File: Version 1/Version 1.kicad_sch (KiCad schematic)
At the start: 82 parts, among them J1 Conn_01x05, Q1 IPP015N04NF2SAKMA1, Q2 IPP015N04NF2SAKMA1, Q3 IPP015N04NF2SAKMA1, Q4 IPP015N04NF2SAKMA1, Q5 IPP015N04NF2SAKMA1, Q6 IPP015N04NF2SAKMA1, U1 TPS62932, U2 TPS62932, U3 TPS62932, U4 IRS2004, U5 IRS2004, U6 IRS2004, U7 YAAJ_BlackPill_SWD_BreakoutV2, U8 Conn_01x01_Socket

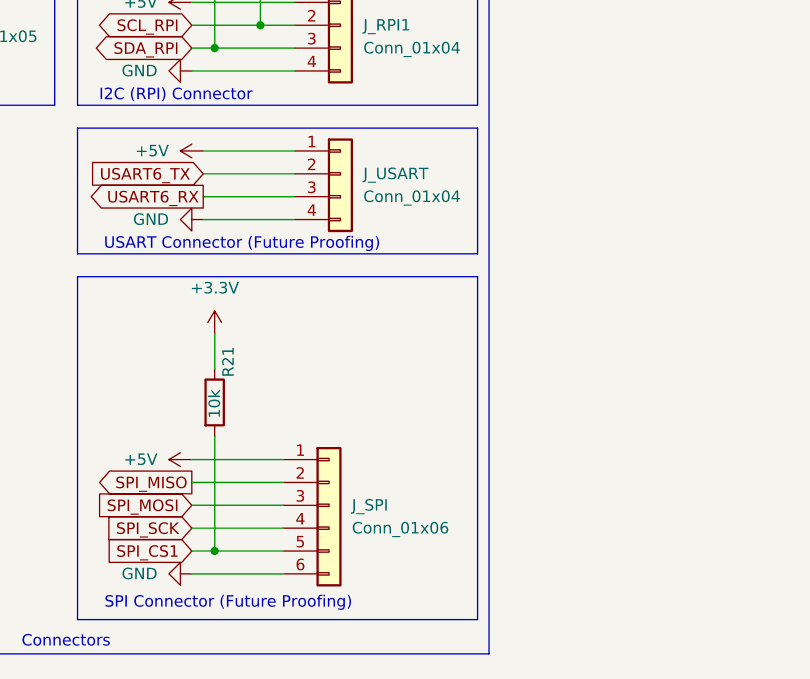
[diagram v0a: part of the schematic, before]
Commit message: Last few changes
Renamed a connector and added proper layout to the schematic.
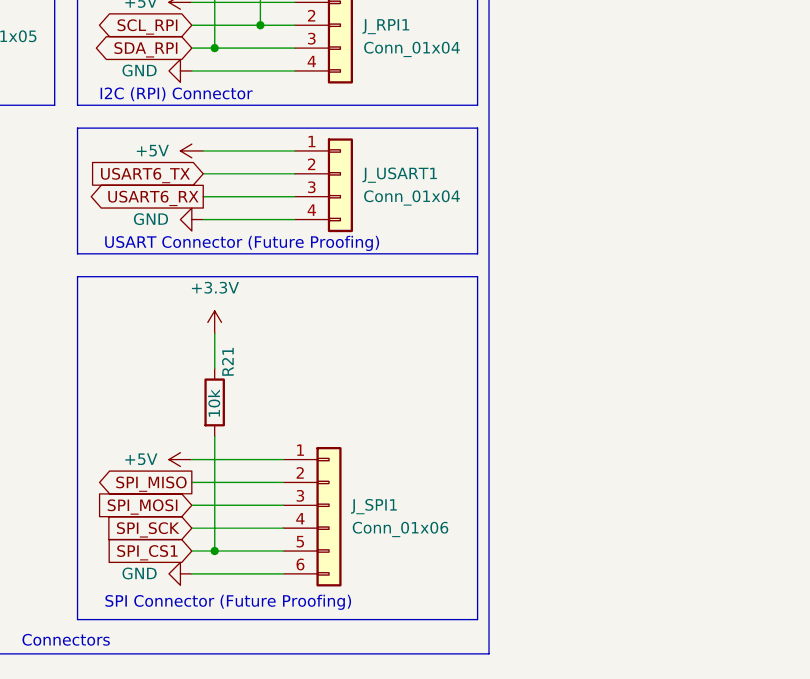
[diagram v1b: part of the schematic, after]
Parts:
- renumbered J_SPI to J_SPI1, J_USART to J_USART1
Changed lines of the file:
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@@
 		(dnp no)
 		(fields_autoplaced yes)
-		(property "Reference" "J_USART"
+		(property "Reference" "J_USART1"
 			(at 173.99 190.4999 0)
 			(effects
@@
 			(project "Version 1"
 				(path "/1b67c1a2-c765-4a1d-8ccd-1a2054fe1222"
-					(reference "J_USART")
+					(reference "J_USART1")
 					(unit 1)
 				)
@@
 		(dnp no)
 		(fields_autoplaced yes)
-		(property "Reference" "J_SPI"
+		(property "Reference" "J_SPI1"
 			(at 172.72 227.3299 0)
 			(effects
@@
 			(project "Version 1"
 				(path "/1b67c1a2-c765-4a1d-8ccd-1a2054fe1222"
-					(reference "J_SPI")
-					(unit 1)
-				)
+					(reference "J_SPI1")
+					(unit 1)
+				)

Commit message: updated footprints and added pos in pcb design
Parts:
- J_RPI1, J_USART1: footprint Connector_JST:JST_ACH_BM04B-ACHSS-A-GAN-ETF_1x04-1MP_P1.20mm_Vertical -> Connector_PinHeader_1.27mm:PinHeader_1x04_P1.27mm_Vertical
- J_SPI1: footprint (none) -> Connector_PinHeader_1.27mm:PinHeader_1x06_P1.27mm_Vertical
- R19, R20, R21: footprint (none) -> Resistor_THT:R_Axial_DIN0207_L6.3mm_D2.5mm_P10.16mm_Horizontal
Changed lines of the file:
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@@
 			)
 		)
-		(property "Footprint" "Connector_JST:JST_ACH_BM04B-ACHSS-A-GAN-ETF_1x04-1MP_P1.20mm_Vertical"
+		(property "Footprint" "Connector_PinHeader_1.27mm:PinHeader_1x04_P1.27mm_Vertical"
 			(at 171.45 190.5 0)
 			(effects
@@
 			)
 		)
-		(property "Footprint" ""
+		(property "Footprint" "Resistor_THT:R_Axial_DIN0207_L6.3mm_D2.5mm_P10.16mm_Horizontal"
 			(at 160.782 165.1 90)
 			(effects
@@
 			)
 		)
-		(property "Footprint" ""
+		(property "Footprint" "Connector_PinHeader_1.27mm:PinHeader_1x06_P1.27mm_Vertical"
 			(at 170.18 227.33 0)
 			(effects
@@
 			)
 		)
-		(property "Footprint" ""
+		(property "Footprint" "Resistor_THT:R_Axial_DIN0207_L6.3mm_D2.5mm_P10.16mm_Horizontal"
 			(at 155.702 165.1 90)
 			(effects
@@
 			)
 		)
-		(property "Footprint" "Connector_JST:JST_ACH_BM04B-ACHSS-A-GAN-ETF_1x04-1MP_P1.20mm_Vertical"
+		(property "Footprint" "Connector_PinHeader_1.27mm:PinHeader_1x04_P1.27mm_Vertical"
 			(at 171.45 173.99 0)
 			(effects
@@
 			)
 		)
-		(property "Footprint" ""
+		(property "Footprint" "Resistor_THT:R_Axial_DIN0207_L6.3mm_D2.5mm_P10.16mm_Horizontal"
 			(at 155.702 215.9 90)
 			(effects

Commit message: updated SCHEMATIC
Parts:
- added C10: 0.1u, symbol Device:C
- added C11: 1n, symbol Device:C
- added U8: ACS712xLCTR-05B, Package_SO:SOIC-8_3.9x4.9mm_P1.27mm, symbol Sensor_Current:ACS712xLCTR-05B
- renumbered U8 to OutU1, V1 to OutW1, W1 to OutW2
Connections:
- net +24V: now also U8.1 (IP+), U8.2 (IP+); no longer C5.1, C7.1, C9.1, Q1.2, Q3.2, Q5.2
- net +5V: now also C10.2, U8.8 (VCC)
- net ADC1: now also U8.7 (VIOUT)
- net GND: now also C10.1, C11.2, U8.5 (GND)
- net SH_U: no longer C4.2, Q1.3, Q2.2
- net SH_V: no longer C6.2, Q3.3, Q4.2
- net SH_W: no longer C8.2, Q5.3, Q6.2
- net at OutW2.1 (Pin_1): now also C8.2, Q5.3, Q6.2
- net at OutW1.1 (Pin_1): now also C6.2, Q3.3, Q4.2
- net at OutU1.1 (Pin_1): now also C4.2, Q1.3, Q2.2
- new net: C11.1, U8.6 (FILTER)
- new net 24V: C5.1, C7.1, C9.1, Q1.2, Q3.2, Q5.2, U8.3 (IP-), U8.4 (IP-)
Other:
- note added: "C12 is a function of the load resistance and filtering desired. R23 can be omitted if the full range is desired"
- note added: "Current sensing"
- moved on the sheet: OutU1, OutW1, OutW2

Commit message: updated
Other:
- note removed: "C12 is a function of the load resistance and filtering desired. R23 can be omitted if the full range is desired"
- moved on the sheet: C10, C11, D1, Jin1, Jout1, U8

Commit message: Nothing
Nothing
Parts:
- Rfbt3: value 30.9 -> 30.9k
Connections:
- net +5V: now also C10.1; no longer C10.2
- net GND: now also C10.2; no longer C10.1
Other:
- moved on the sheet: C10
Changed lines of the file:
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@@
 	)
 	(junction
-		(at 273.05 93.98)
+		(at 96.52 33.02)
 		(diameter 0)
 		(color 0 0 0 0)
 	)
 	(junction
-		(at 96.52 33.02)
+		(at 87.63 83.82)
 		(diameter 0)
 		(color 0 0 0 0)
 	)
 	(junction
-		(at 87.63 83.82)
+		(at 273.05 90.17)
 		(diameter 0)
 		(color 0 0 0 0)
@@
 	(wire
 		(pts
+			(xy 283.21 91.44) (xy 283.21 90.17)
+		)
+		(stroke
+			(width 0)
+			(type default)
+		)
+	)
+	(wire
+		(pts
 			(xy 166.37 187.96) (xy 156.21 187.96)
 		)
@@
 	(wire
 		(pts
-			(xy 271.78 93.98) (xy 273.05 93.98)
-		)
-		(stroke
-			(width 0)
-			(type default)
-		)
-	)
-	(wire
-		(pts
 			(xy 330.2 43.18) (xy 330.2 46.99)
 		)
@@
 	(wire
 		(pts
+			(xy 273.05 90.17) (xy 273.05 95.25)
+		)
+		(stroke
+			(width 0)
+			(type default)
+		)
+	)
+	(wire
+		(pts
 			(xy 30.48 120.65) (xy 30.48 121.92)
 		)
@@
 	(wire
 		(pts
+			(xy 274.32 90.17) (xy 273.05 90.17)
+		)
+		(stroke
+			(width 0)
+			(type default)
+		)
+	)
+	(wire
+		(pts
 			(xy 175.26 46.99) (xy 175.26 50.8)
 		)
@@
 	(wire
 		(pts
-			(xy 273.05 92.71) (xy 273.05 93.98)
-		)
-		(stroke
-			(width 0)
-			(type default)
-		)
-	)
-	(wire
-		(pts
 			(xy 25.4 121.92) (xy 30.48 121.92)
 		)
@@
 	(wire
 		(pts
-			(xy 273.05 93.98) (xy 273.05 95.25)
+			(xy 148.59 86.36) (xy 148.59 88.9)
 		)
 		(stroke
@@
 	(wire
 		(pts
-			(xy 148.59 86.36) (xy 148.59 88.9)
+			(xy 29.21 34.29) (xy 29.21 35.56)
 		)
 		(stroke
@@
 	(wire
 		(pts
-			(xy 29.21 34.29) (xy 29.21 35.56)
+			(xy 173.99 115.57) (xy 173.99 116.84)
 		)
 		(stroke
@@
 	(wire
 		(pts
-			(xy 173.99 115.57) (xy 173.99 116.84)
+			(xy 283.21 90.17) (xy 281.94 90.17)
 		)
 		(stroke
@@
 		(on_board yes)
 		(dnp no)
-		(fields_autoplaced yes)
 		(property "Reference" "#PWR029"
 			(at 212.09 88.9 0)
@@
 	(symbol
 		(lib_id "Device:C")
-		(at 273.05 88.9 0)
+		(at 278.13 90.17 90)
 		(unit 1)
 		(exclude_from_sim no)
@@
 		(on_board yes)
 		(dnp no)
-		(fields_autoplaced yes)
 		(property "Reference" "C10"
-			(at 276.86 87.6299 0)
+			(at 278.384 84.836 90)
 			(effects
 				(font
 					(size 1.27 1.27)
 				)
-				(justify left)
 			)
 		)
 		(property "Value" "0.1u"
-			(at 276.86 90.1699 0)
+			(at 278.384 86.868 90)
 			(effects
 				(font
 					(size 1.27 1.27)
 				)
-				(justify left)
 			)
 		)
 		(property "Footprint" ""
-			(at 274.0152 92.71 0)
+			(at 281.94 89.2048 0)
 			(effects
 				(font
@@
 		)
 		(property "Datasheet" "~"
-			(at 273.05 88.9 0)
+			(at 278.13 90.17 0)
 			(effects
 				(font
@@
 		)
 		(property "Description" "Unpolarized capacitor"
-			(at 273.05 88.9 0)
+			(at 278.13 90.17 0)
 			(effects
 				(font
@@
 		(lib_name "+5V_3")
 		(lib_id "power:+5V")
-		(at 271.78 93.98 90)
+		(at 273.05 90.17 0)
 		(unit 1)
 		(exclude_from_sim no)
@@
 		(on_board yes)
 		(dnp no)
-		(fields_autoplaced yes)
 		(property "Reference" "#PWR033"
-			(at 275.59 93.98 0)
+			(at 273.05 93.98 0)
 			(effects
 				(font
@@
 		)
 		(property "Value" "+5V"
-			(at 267.97 93.9799 90)
+			(at 270.764 86.36 0)
 			(effects
 				(font
@@
 		)
 		(property "Footprint" ""
-			(at 271.78 93.98 0)
+			(at 273.05 90.17 0)
 			(effects
 				(font
@@
 		)
 		(property "Datasheet" ""
-			(at 271.78 93.98 0)
+			(at 273.05 90.17 0)
 			(effects
 				(font
@@
 		)
 		(property "Description" "Power symbol creates a global label with name \"+5V\""
-			(at 271.78 93.98 0)
+			(at 273.05 90.17 0)
 			(effects
 				(font
@@
 		(lib_name "GND_7")
 		(lib_id "power:GND")
-		(at 273.05 85.09 180)
+		(at 283.21 91.44 0)
 		(unit 1)
 		(exclude_from_sim no)
@@
 		(fields_autoplaced yes)
 		(property "Reference" "#PWR036"
-			(at 273.05 78.74 0)
+			(at 283.21 97.79 0)
 			(effects
 				(font
@@
 		)
 		(property "Value" "GND"
-			(at 273.05 80.01 0)
+			(at 285.75 92.7099 0)
 			(effects
 				(font
 					(size 1.27 1.27)
 				)
+				(justify left)
 			)
 		)
 		(property "Footprint" ""
-			(at 273.05 85.09 0)
+			(at 283.21 91.44 0)
 			(effects
 				(font
@@
 		)
 		(property "Datasheet" ""
-			(at 273.05 85.09 0)
+			(at 283.21 91.44 0)
 			(effects
 				(font
@@
 		)
 		(property "Description" "Power symbol creates a global label with name \"GND\" , ground"
-			(at 273.05 85.09 0)
+			(at 283.21 91.44 0)
 			(effects
 				(font
@@
 		(on_board yes)
 		(dnp no)
-		(fields_autoplaced yes)
 		(property "Reference" "Rfbt3"
-			(at 87.63 123.19 0)
+			(at 86.614 122.428 0)
 			(effects
 				(font
@@
 			)
 		)
-		(property "Value" "30.9"
-			(at 87.63 124.46 0)
+		(property "Value" "30.9k"
+			(at 86.868 124.714 0)
 			(effects
 				(font
@@
 		(on_board yes)
 		(dnp no)
-		(fields_autoplaced yes)
 		(property "Reference" "U8"
-			(at 275.2441 92.71 0)
+			(at 271.526 104.902 0)
 			(effects
 				(font
@@
 		)
 		(property "Value" "ACS712xLCTR-05B"
-			(at 275.2441 95.25 0)
+			(at 274.828 96.774 0)
 			(effects
 				(font
